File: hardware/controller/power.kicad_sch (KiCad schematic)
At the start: 16 parts, among them J11 Barrel_Jack, J7 Conn_01x04_Pin, J8 Conn_01x04_Pin, U7 MPM3606AGQV-P, U8 LM73100RPWR, U9 LM73100RPWR

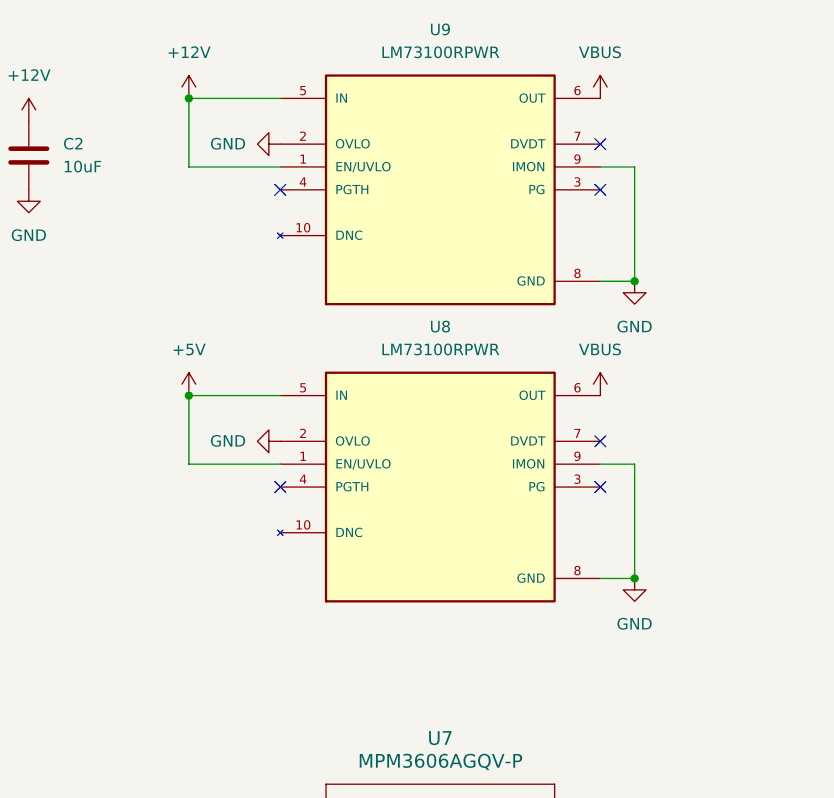
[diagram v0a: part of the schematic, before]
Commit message: Replace input diodes with power mux chip
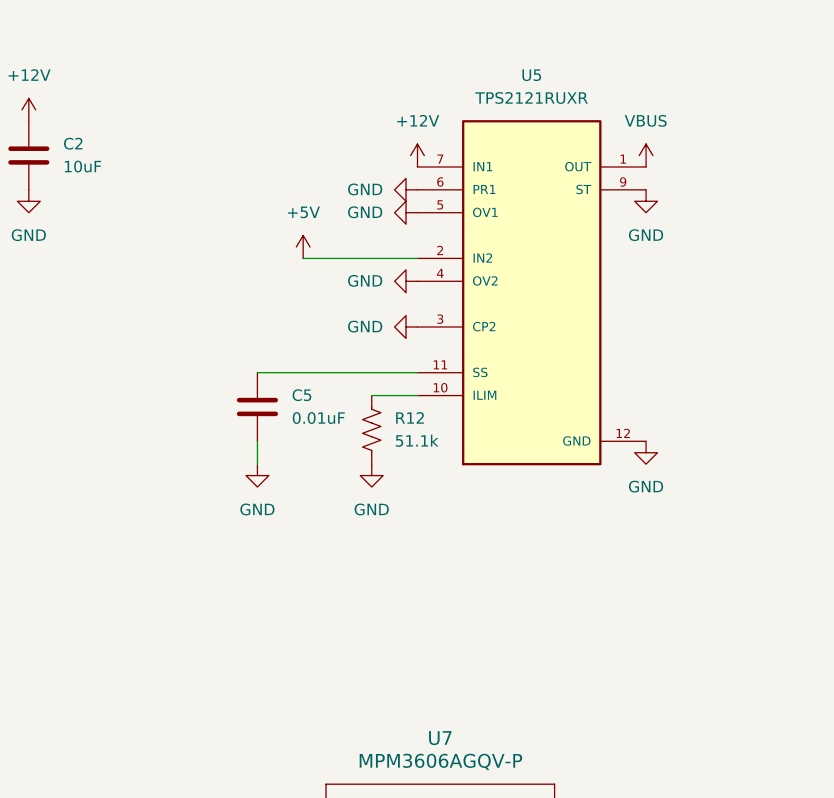
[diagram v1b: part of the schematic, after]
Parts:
- removed U8, U9: LM73100RPWR, LM73100:IC_LM73100RPWR, symbol LM73100:LM73100RPWR
- added C5: 0.01uF, Capacitor_SMD:C_0805_2012Metric, symbol Device:C
- added R12: 51.1k, Resistor_SMD:R_0805_2012Metric, symbol Device:R_US
- added U5: TPS2121RUXR, TPS2121RUXR:IC_TPS2121RUXR, symbol TPS2121:TPS2121RUXR
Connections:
- net +12V: now also U5.7 (IN1), U5.7_1 (IN1)
- net +5V: now also U5.2 (IN2), U5.2_1 (IN2)
- net GND: now also C5.2, R12.2, U5.12 (GND), U5.3 (CP2), U5.4 (OV2), U5.5 (OV1), U5.6 (PR1), U5.9 (ST)
- net VBUS: now also U5.1 (OUT), U5.1_1 (OUT), U5.8 (OUT), U5.8_1 (OUT)
- new net: R12.1, U5.10 (ILIM)
- new net: C5.1, U5.11 (SS)
- no-connect marks 10 -> 4

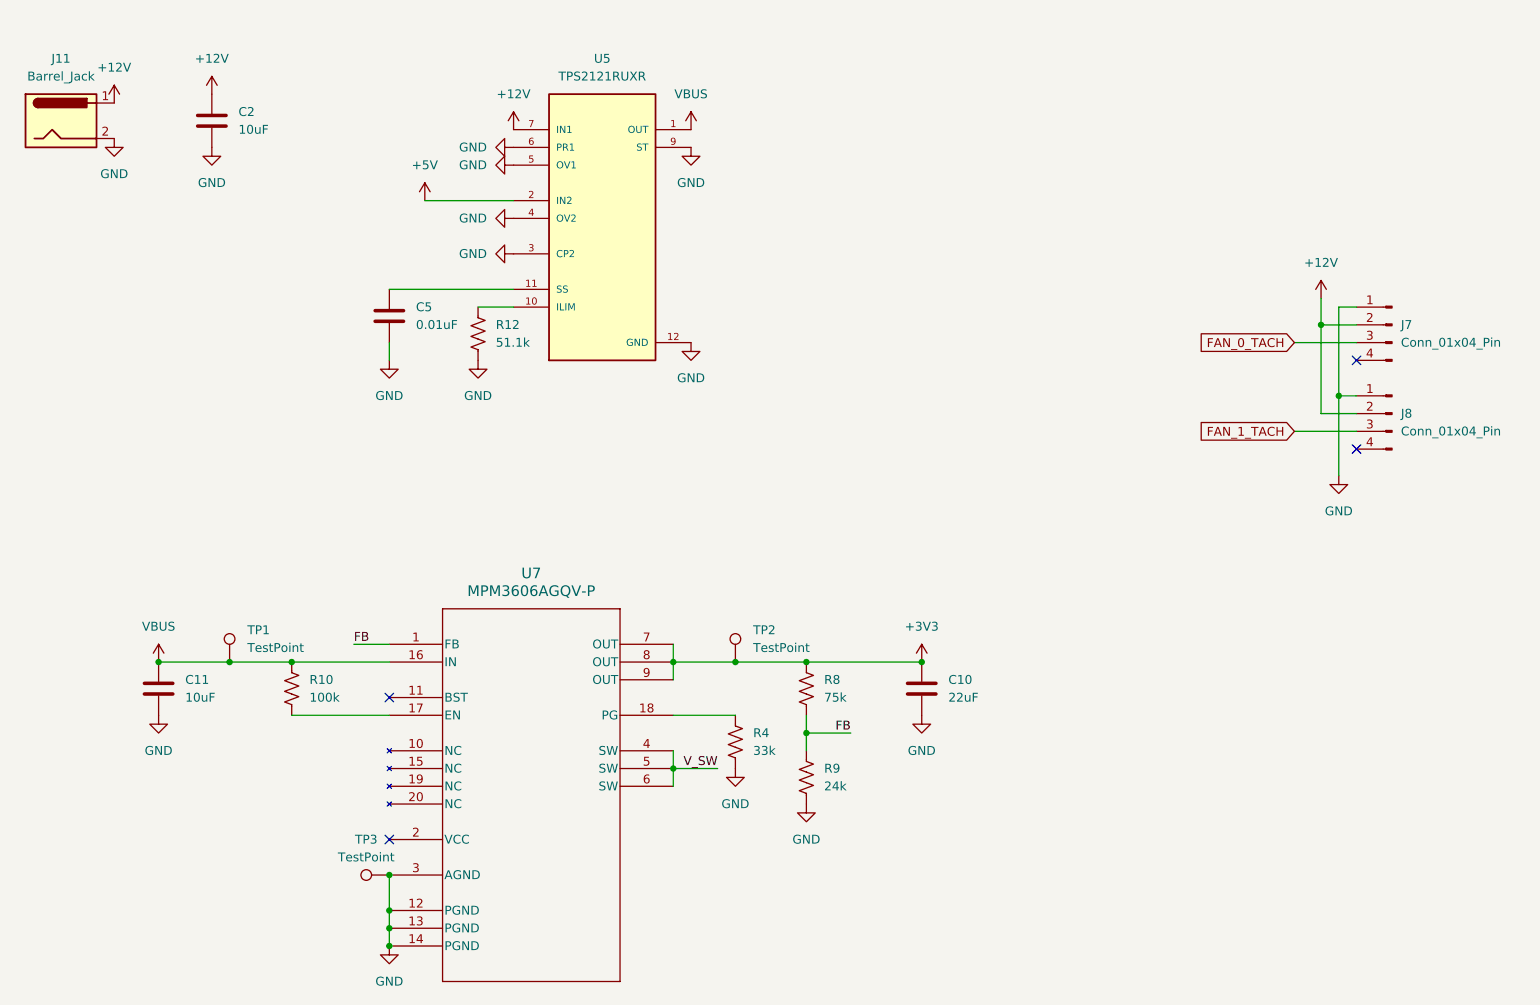
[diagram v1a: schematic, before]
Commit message: Swap out voltage regulator
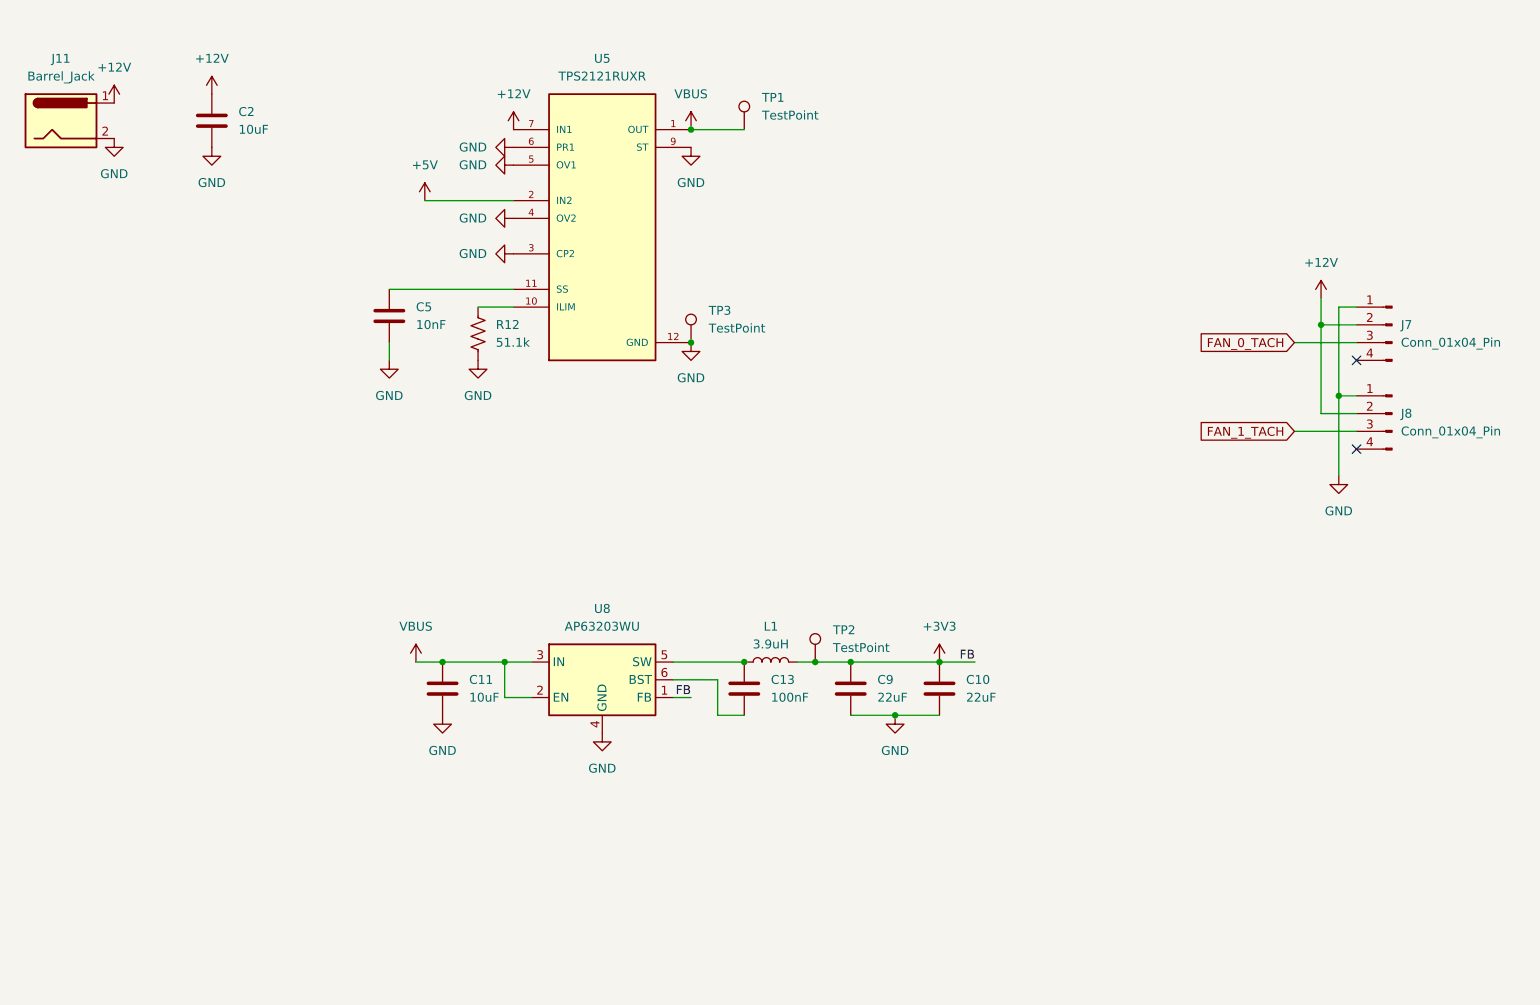
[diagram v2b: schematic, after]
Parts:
- removed R10: 100k, Resistor_SMD:R_0805_2012Metric, symbol Device:R_US
- removed R4: 33k, Resistor_SMD:R_0805_2012Metric, symbol Device:R_US
- removed R8: 75k, Resistor_SMD:R_0805_2012Metric, symbol Device:R_US
- removed R9: 24k, Resistor_SMD:R_0805_2012Metric, symbol Device:R_US
- removed U7: MPM3606AGQV-P, MPM3606:QFN3p0x5p0x1p6_MPM3606A_MNP, symbol MPM3606:MPM3606AGQV-P
- added C13: 100nF, Capacitor_SMD:C_0805_2012Metric, symbol Device:C
- added C9: 22uF, Capacitor_SMD:C_0805_2012Metric, symbol Device:C
- added L1: 3.9uH, Inductor_SMD:L_0805_2012Metric, symbol Device:L
- added U8: AP63203WU, Package_TO_SOT_SMD:TSOT-23-6, symbol Regulator_Switching:AP63203WU
- C10: LCSC C602037 -> C5674
- C5: value 0.01uF -> 10nF; LCSC (none) -> C1710
- R12: LCSC (none) -> C17731
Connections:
- net +3V3: now also C9.1, L1.2, U8.1 (FB)
- net GND: now also C9.2, U8.4 (GND)
- net VBUS: now also U8.2 (EN), U8.3 (IN)
- new net: C13.1, L1.1, U8.5 (SW)
- new net: C13.2, U8.6 (BST)
- no-connect marks 4 -> 2
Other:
- moved on the sheet: C11, TP1, TP2, TP3

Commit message: Update inductor to match regulator spec better
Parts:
- L1: footprint Inductor_SMD:L_0805_2012Metric -> Inductor_SMD:L_APV_ANR3015; LCSC C69486 -> C42429305
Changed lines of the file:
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@@
 			)
 		)
-		(property "Footprint" "Inductor_SMD:L_0805_2012Metric"
+		(property "Footprint" "Inductor_SMD:L_APV_ANR3015"
 			(at 133.35 115.57 0)
 			(effects
@@
 			)
 		)
-		(property "LCSC" "C69486"
+		(property "LCSC" "C42429305"
 			(at 133.35 115.57 90)
 			(effects

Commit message: 1.1 production tweaks
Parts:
- U8: FT Rotation Offset (none) -> 90
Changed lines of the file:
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@@
+			)
+		)
+		(property "FT Rotation Offset" "90"
+			(at 109.22 118.11 0)
+			(effects
+				(font
+					(size 1.27 1.27)
+				)
+				(hide yes)
 			)
 		)

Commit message: Protect fan tach inputs
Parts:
- TP1, TP2, TP3: now left out of the parts list
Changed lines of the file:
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@@
 		(unit 1)
 		(exclude_from_sim no)
-		(in_bom yes)
+		(in_bom no)
 		(on_board yes)
 		(dnp no)
@@
 		(unit 1)
 		(exclude_from_sim no)
-		(in_bom yes)
+		(in_bom no)
 		(on_board yes)
 		(dnp no)
@@
 		(unit 1)
 		(exclude_from_sim no)
-		(in_bom yes)
-		(on_board yes)
-		(dnp no)
+		(in_bom no)
+		(on_board yes)
+		(dnp no)

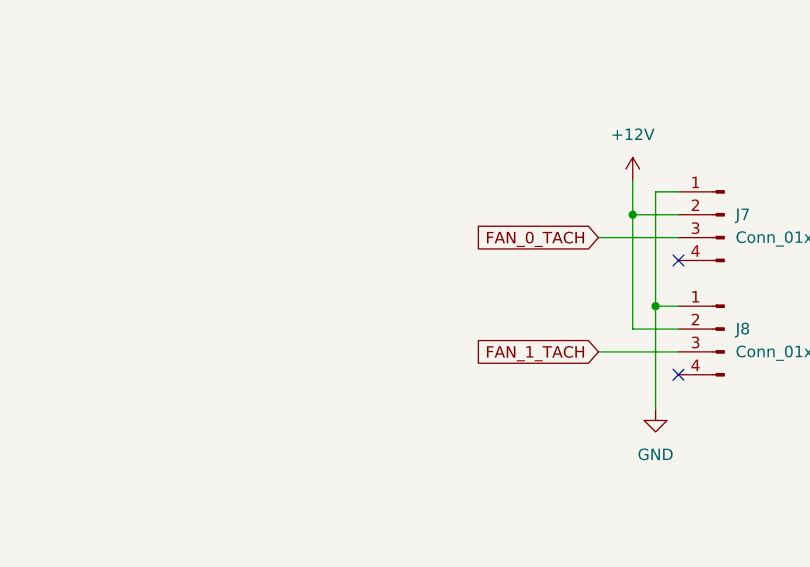
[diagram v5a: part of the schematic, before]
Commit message: Add TVS diode to 12V rail
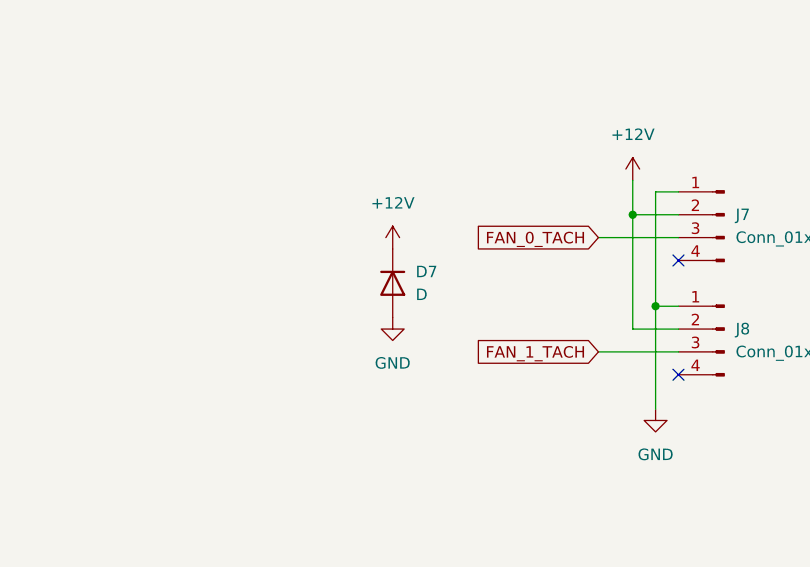
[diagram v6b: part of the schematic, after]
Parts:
- added D7: D, Diode_SMD:D_SMA, symbol Device:D
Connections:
- net +12V: now also D7.1 (K)
- net GND: now also D7.2 (A)
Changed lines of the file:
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@@
+	)
+	(symbol
+		(lib_id "Device:D")
+		(at 185.42 74.93 270)
+		(unit 1)
+		(exclude_from_sim no)
+		(in_bom yes)
+		(on_board yes)
+		(dnp no)
+		(fields_autoplaced yes)
+		(property "Reference" "D7"
+			(at 187.96 73.6599 90)
+			(effects
+				(font
+					(size 1.27 1.27)
+				)
+				(justify left)
+			)
+		)
+		(property "Value" "D"
+			(at 187.96 76.1999 90)
+			(effects
+				(font
+					(size 1.27 1.27)
+				)
+				(justify left)
+			)
+		)
+		(property "Footprint" "Diode_SMD:D_SMA"
+			(at 185.42 74.93 0)
+			(effects
+				(font
+					(size 1.27 1.27)
+				)
+				(hide yes)
+			)
+		)
+		(property "Datasheet" "~"
+			(at 185.42 74.93 0)
+			(effects
+				(font
+					(size 1.27 1.27)
+				)
+				(hide yes)
+			)
+		)
+		(property "Description" "Diode"
+			(at 185.42 74.93 0)
+			(effects
+				(font
+					(size 1.27 1.27)
+				)
+				(hide yes)
+			)
+		)
+		(property "Sim.Device" "D"
+			(at 185.42 74.93 0)
+			(effects
+				(font
+					(size 1.27 1.27)
+				)
+				(hide yes)
+			)
+		)
+		(property "Sim.Pins" "1=K 2=A"
+			(at 185.42 74.93 0)
+			(effects
+				(font
+					(size 1.27 1.27)
+				)
+				(hide yes)
+			)
+		)
+		(property "LCSC" "C445494"
+			(at 185.42 74.93 90)
+			(effects
+				(font
+					(size 1.27 1.27)
+				)
+				(hide yes)
+			)
+		)
+		(pin "2"
+		)
+		(pin "1"
+		)
+		(instances
+			(project ""
+				(path "/3ee12552-bbaf-4643-8241-99077a41063f/dc443349-7fb4-42c6-a18e-09a219bb9ecd"
+					(reference "D7")
+					(unit 1)
+				)
+			)
+		)
 	)
 	(symbol
@@
 	(symbol
 		(lib_id "power:GND")
+		(at 185.42 78.74 0)
+		(unit 1)
+		(exclude_from_sim no)
+		(in_bom yes)
+		(on_board yes)
+		(dnp no)
+		(fields_autoplaced yes)
+		(property "Reference" "#PWR0103"
+			(at 185.42 85.09 0)
+			(effects
+				(font
+					(size 1.27 1.27)
+				)
+				(hide yes)
+			)
+		)
+		(property "Value" "GND"
+			(at 185.42 83.82 0)
+			(effects
+				(font
+					(size 1.27 1.27)
+				)
+			)
+		)
+		(property "Footprint" ""
+			(at 185.42 78.74 0)
+			(effects
+				(font
+					(size 1.27 1.27)
+				)
+				(hide yes)
+			)
+		)
+		(property "Datasheet" ""
+			(at 185.42 78.74 0)
+			(effects
+				(font
+					(size 1.27 1.27)
+				)
+				(hide yes)
+			)
+		)
+		(property "Description" "Power symbol creates a global label with name \"GND\" , ground"
+			(at 185.42 78.74 0)
+			(effects
+				(font
+					(size 1.27 1.27)
+				)
+				(hide yes)
+			)
+		)
+		(pin "1"
+		)
+		(instances
+			(project "controller"
+				(path "/3ee12552-bbaf-4643-8241-99077a41063f/dc443349-7fb4-42c6-a18e-09a219bb9ecd"
+					(reference "#PWR0103")
+					(unit 1)
+				)
+			)
+		)
+	)
+	(symbol
+		(lib_id "power:GND")
 		(at 96.52 52.07 270)
 		(unit 1)
@@
 					(unit 1)
 				)
+			)
+		)
+	)
+	(symbol
+		(lib_id "power:+12V")
+		(at 185.42 71.12 0)
+		(unit 1)
+		(exclude_from_sim no)
+		(in_bom yes)
+		(on_board yes)
+		(dnp no)
+		(fields_autoplaced yes)
+		(property "Reference" "#PWR043"
+			(at 185.42 74.93 0)
+			(effects
+				(font
+					(size 1.27 1.27)
+				)
+				(hide yes)
+			)
+		)
+		(property "Value" "+12V"
+			(at 185.42 66.04 0)
+			(effects
+				(font
+					(size 1.27 1.27)
+				)
+			)
+		)
+		(property "Footprint" ""
+			(at 185.42 71.12 0)
+			(effects
+				(font
+					(size 1.27 1.27)
+				)
+				(hide yes)
+			)
+		)
+		(property "Datasheet" ""
+			(at 185.42 71.12 0)
+			(effects
+				(font
+					(size 1.27 1.27)
+				)
+				(hide yes)
+			)
+		)
+		(property "Description" "Power symbol creates a global label with name \"+12V\""
+			(at 185.42 71.12 0)
+			(effects
+				(font
+					(size 1.27 1.27)
+				)
+				(hide yes)
+			)
+		)
+		(pin "1"
+		)
+		(instances
+			(project "controller"
+				(path "/3ee12552-bbaf-4643-8241-99077a41063f/dc443349-7fb4-42c6-a18e-09a219bb9ecd"
+					(reference "#PWR043")
+					(unit 1)
+				)

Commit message: Fix power mux rotation
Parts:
- U5: FT Rotation Offset (none) -> 270
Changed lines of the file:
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@@
+			)
+		)
+		(property "FT Rotation Offset" "270"
+			(at 109.22 54.61 0)
+			(effects
+				(font
+					(size 1.27 1.27)
+				)
+				(hide yes)
 			)
 		)
